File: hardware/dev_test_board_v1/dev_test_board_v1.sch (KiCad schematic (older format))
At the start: 52 parts, among them J1 USB_B_Micro, J2 Conn_SWD, J3 Conn_LCD, J4 Conn_GP, SW1 SW_SPDT, SW2 SW_PUSH, SW3 SW_PUSH, SW4 SW_PUSH, U1 STM32L031C4Tx, U2 FT230XS, U3 LIS2HH12, Y1 8MHz

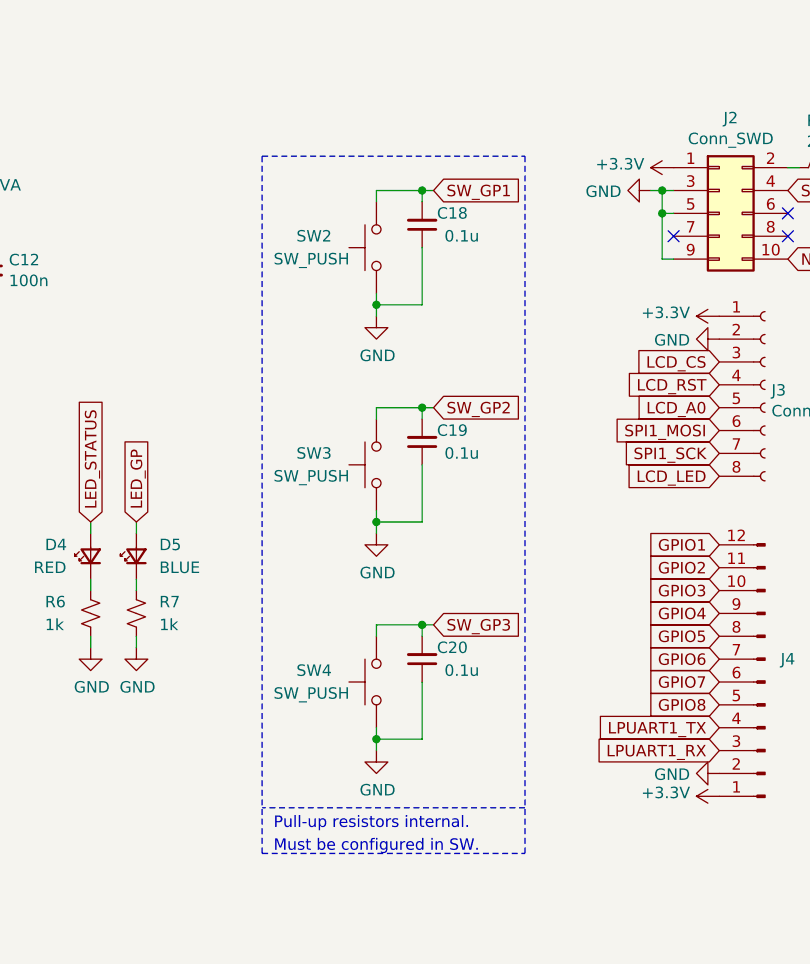
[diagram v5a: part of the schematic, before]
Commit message: Removed HW debouncing for SW2-4, finished routing.
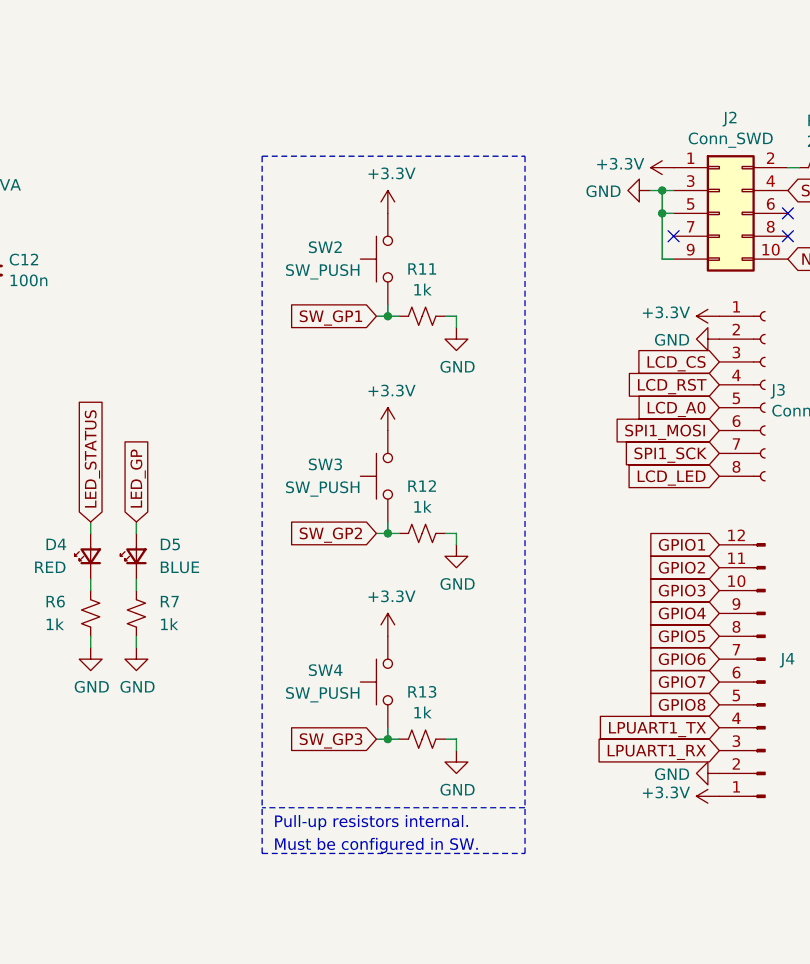
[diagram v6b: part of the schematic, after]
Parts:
- removed C18, C19, C20: 0.1u, Capacitor_SMD:C_0603_1608Metric, symbol Device:C_Small
- added R11, R12, R13: 1k, Resistor_SMD:R_0402_1005Metric, symbol Device:R_Small_US
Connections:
- net +3V3: now also SW2.2, SW3.2, SW4.2
- net GND: now also R11.1, R12.1, R13.1; no longer SW2.1, SW3.1, SW4.1
- net SW_GP1: now also SW2.1, R11.2; no longer SW2.2
- net SW_GP2: now also SW3.1, R12.2; no longer SW3.2
- net SW_GP3: now also SW4.1, R13.2; no longer SW4.2
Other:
- moved on the sheet: SW2
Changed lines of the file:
@@
 Text GLabel 10050 4700 0    50   Input ~ 0
 GPIO1
-Text GLabel 8800 5050 2    50   Input ~ 0
-SW_GP3
-$Comp
-L power:GND #PWR0140
-U 1 1 60A74DE7
-P 8550 5600
-F 0 "#PWR0140" H 8550 5350 50  0001 C CNN
-F 1 "GND" H 8555 5427 50  0000 C CNN
-F 2 "" H 8550 5600 50  0001 C CNN
-F 3 "" H 8550 5600 50  0001 C CNN
-	1    8550 5600
-	1    0    0    -1
-$EndComp
-Connection ~ 8550 5550
-Wire Wire Line
-	8550 5550 8550 5600
-Wire Wire Line
-	8750 5550 8550 5550
-Wire Wire Line
-	8750 5300 8750 5550
-Connection ~ 8750 5050
-Wire Wire Line
-	8750 5050 8800 5050
-Wire Wire Line
-	8750 5050 8750 5100
-Wire Wire Line
-	8550 5050 8750 5050
-Wire Wire Line
-	8550 5100 8550 5050
-Wire Wire Line
-	8550 5500 8550 5550
-$Comp
-L Switch:SW_Push SW4
-U 1 1 60A74DD7
-P 8550 5300
-F 0 "SW4" V 8600 5650 50  0000 R CNN
-F 1 "SW_PUSH" V 8500 5750 50  0000 R CNN
-F 2 "Button_Switch_SMD:SW_Push_1P1T_NO_6x6mm_H9.5mm" H 8550 5500 50  0001 C CNN
-F 3 "~" H 8550 5500 50  0001 C CNN
-	1    8550 5300
-	0    -1   -1   0
-$EndComp
-$Comp
-L Device:C_Small C20
-U 1 1 60A74DD1
-P 8750 5200
-F 0 "C20" H 8550 5150 50  0000 L CNN
-F 1 "0.1u" H 8500 5250 50  0000 L CNN
-F 2 "Capacitor_SMD:C_0603_1608Metric" H 8750 5200 50  0001 C CNN
-F 3 "~" H 8750 5200 50  0001 C CNN
-	1    8750 5200
-	-1   0    0    1
-$EndComp
-Text GLabel 8800 4100 2    50   Input ~ 0
-SW_GP2
-$Comp
-L power:GND #PWR0139
-U 1 1 60A5AFB5
-P 8550 4650
-F 0 "#PWR0139" H 8550 4400 50  0001 C CNN
-F 1 "GND" H 8555 4477 50  0000 C CNN
-F 2 "" H 8550 4650 50  0001 C CNN
-F 3 "" H 8550 4650 50  0001 C CNN
-	1    8550 4650
-	1    0    0    -1
-$EndComp
-Connection ~ 8550 4600
-Wire Wire Line
-	8550 4600 8550 4650
-Wire Wire Line
-	8750 4600 8550 4600
-Wire Wire Line
-	8750 4350 8750 4600
-Connection ~ 8750 4100
-Wire Wire Line
-	8750 4100 8800 4100
-Wire Wire Line
-	8750 4100 8750 4150
-Wire Wire Line
-	8550 4100 8750 4100
-Wire Wire Line
-	8550 4150 8550 4100
-Wire Wire Line
-	8550 4550 8550 4600
-$Comp
-L Switch:SW_Push SW3
-U 1 1 60A5AFA5
-P 8550 4350
-F 0 "SW3" V 8600 4700 50  0000 R CNN
-F 1 "SW_PUSH" V 8500 4800 50  0000 R CNN
-F 2 "Button_Switch_SMD:SW_Push_1P1T_NO_6x6mm_H9.5mm" H 8550 4550 50  0001 C CNN
-F 3 "~" H 8550 4550 50  0001 C CNN
-	1    8550 4350
-	0    -1   -1   0
-$EndComp
-$Comp
-L Device:C_Small C19
-U 1 1 60A5AF9F
-P 8750 4250
-F 0 "C19" H 8550 4200 50  0000 L CNN
-F 1 "0.1u" H 8500 4300 50  0000 L CNN
-F 2 "Capacitor_SMD:C_0603_1608Metric" H 8750 4250 50  0001 C CNN
-F 3 "~" H 8750 4250 50  0001 C CNN
-	1    8750 4250
-	-1   0    0    1
-$EndComp
-Text GLabel 8800 3150 2    50   Input ~ 0
+Text GLabel 8550 3700 0    50   Input ~ 0
 SW_GP1
-$Comp
-L power:GND #PWR0138
-U 1 1 60A551CE
-P 8550 3700
-F 0 "#PWR0138" H 8550 3450 50  0001 C CNN
-F 1 "GND" H 8555 3527 50  0000 C CNN
-F 2 "" H 8550 3700 50  0001 C CNN
-F 3 "" H 8550 3700 50  0001 C CNN
-	1    8550 3700
-	1    0    0    -1
-$EndComp
-Connection ~ 8550 3650
-Wire Wire Line
-	8550 3650 8550 3700
-Wire Wire Line
-	8750 3650 8550 3650
-Wire Wire Line
-	8750 3400 8750 3650
-Connection ~ 8750 3150
-Wire Wire Line
-	8750 3150 8800 3150
-Wire Wire Line
-	8750 3150 8750 3200
-Wire Wire Line
-	8550 3150 8750 3150
-Wire Wire Line
-	8550 3200 8550 3150
-Wire Wire Line
-	8550 3600 8550 3650
 $Comp
 L Switch:SW_Push SW2
 U 1 1 60A2B615
-P 8550 3400
-F 0 "SW2" V 8600 3750 50  0000 R CNN
-F 1 "SW_PUSH" V 8500 3850 50  0000 R CNN
-F 2 "Button_Switch_SMD:SW_Push_1P1T_NO_6x6mm_H9.5mm" H 8550 3600 50  0001 C CNN
-F 3 "~" H 8550 3600 50  0001 C CNN
-	1    8550 3400
+P 8600 3450
+F 0 "SW2" V 8650 3800 50  0000 R CNN
+F 1 "SW_PUSH" V 8550 3900 50  0000 R CNN
+F 2 "Button_Switch_SMD:SW_Push_1P1T_NO_6x6mm_H9.5mm" H 8600 3650 50  0001 C CNN
+F 3 "~" H 8600 3650 50  0001 C CNN
+	1    8600 3450
 	0    -1   -1   0
 $EndComp
@@
 	1    9850 3050
 	0    -1   -1   0
-$EndComp
-$Comp
-L Device:C_Small C18
-U 1 1 609CE345
-P 8750 3300
-F 0 "C18" H 8550 3250 50  0000 L CNN
-F 1 "0.1u" H 8500 3350 50  0000 L CNN
-F 2 "Capacitor_SMD:C_0603_1608Metric" H 8750 3300 50  0001 C CNN
-F 3 "~" H 8750 3300 50  0001 C CNN
-	1    8750 3300
-	-1   0    0    1
 $EndComp
 Text GLabel 10350 3450 2    50   Input ~ 0
@@
 Wire Wire Line
 	3100 1300 3100 1400
+$Comp
+L power:+3.3V #PWR0139
+U 1 1 60A33A90
+P 8600 3250
+F 0 "#PWR0139" H 8600 3100 50  0001 C CNN
+F 1 "+3.3V" H 8615 3423 50  0000 C CNN
+F 2 "" H 8600 3250 50  0001 C CNN
+F 3 "" H 8600 3250 50  0001 C CNN
+	1    8600 3250
+	1    0    0    -1
+$EndComp
+Wire Wire Line
+	8600 3650 8600 3700
+Wire Wire Line
+	8600 3700 8650 3700
+Wire Wire Line
+	8850 3700 8900 3700
+Wire Wire Line
+	8900 3700 8900 3750
+$Comp
+L power:GND #PWR0140
+U 1 1 60A5CE5A
+P 8900 3750
+F 0 "#PWR0140" H 8900 3500 50  0001 C CNN
+F 1 "GND" H 8905 3577 50  0000 C CNN
+F 2 "" H 8900 3750 50  0001 C CNN
+F 3 "" H 8900 3750 50  0001 C CNN
+	1    8900 3750
+	1    0    0    -1
+$EndComp
+Text GLabel 8550 4650 0    50   Input ~ 0
+SW_GP2
+$Comp
+L Switch:SW_Push SW3
+U 1 1 60A82445
+P 8600 4400
+F 0 "SW3" V 8650 4750 50  0000 R CNN
+F 1 "SW_PUSH" V 8550 4850 50  0000 R CNN
+F 2 "Button_Switch_SMD:SW_Push_1P1T_NO_6x6mm_H9.5mm" H 8600 4600 50  0001 C CNN
+F 3 "~" H 8600 4600 50  0001 C CNN
+	1    8600 4400
+	0    -1   -1   0
+$EndComp
+$Comp
+L power:+3.3V #PWR0146
+U 1 1 60A8244B
+P 8600 4200
+F 0 "#PWR0146" H 8600 4050 50  0001 C CNN
+F 1 "+3.3V" H 8615 4373 50  0000 C CNN
+F 2 "" H 8600 4200 50  0001 C CNN
+F 3 "" H 8600 4200 50  0001 C CNN
+	1    8600 4200
+	1    0    0    -1
+$EndComp
+Wire Wire Line
+	8600 4600 8600 4650
+Wire Wire Line
+	8600 4650 8650 4650
+Connection ~ 8600 4650
+$Comp
+L Device:R_Small_US R12
+U 1 1 60A82455
+P 8750 4650
+F 0 "R12" V 8545 4650 50  0000 C CNN
+F 1 "1k" V 8636 4650 50  0000 C CNN
+F 2 "Resistor_SMD:R_0402_1005Metric" H 8750 4650 50  0001 C CNN
+F 3 "~" H 8750 4650 50  0001 C CNN
+	1    8750 4650
+	0    1    1    0
+$EndComp
+Wire Wire Line
+	8850 4650 8900 4650
+Wire Wire Line
+	8900 4650 8900 4700
+$Comp
+L power:GND #PWR0147
+U 1 1 60A8245D
+P 8900 4700
+F 0 "#PWR0147" H 8900 4450 50  0001 C CNN
+F 1 "GND" H 8905 4527 50  0000 C CNN
+F 2 "" H 8900 4700 50  0001 C CNN
+F 3 "" H 8900 4700 50  0001 C CNN
+	1    8900 4700
+	1    0    0    -1
+$EndComp
+Text GLabel 8550 5550 0    50   Input ~ 0
+SW_GP3
+$Comp
+L Switch:SW_Push SW4
+U 1 1 60A9BB90
+P 8600 5300
+F 0 "SW4" V 8650 5650 50  0000 R CNN
+F 1 "SW_PUSH" V 8550 5750 50  0000 R CNN
+F 2 "Button_Switch_SMD:SW_Push_1P1T_NO_6x6mm_H9.5mm" H 8600 5500 50  0001 C CNN
+F 3 "~" H 8600 5500 50  0001 C CNN
+	1    8600 5300
+	0    -1   -1   0
+$EndComp
+$Comp
+L power:+3.3V #PWR0149
+U 1 1 60A9BB96
+P 8600 5100
+F 0 "#PWR0149" H 8600 4950 50  0001 C CNN
+F 1 "+3.3V" H 8615 5273 50  0000 C CNN
+F 2 "" H 8600 5100 50  0001 C CNN
+F 3 "" H 8600 5100 50  0001 C CNN
+	1    8600 5100
+	1    0    0    -1
+$EndComp
+Wire Wire Line
+	8600 5500 8600 5550
+Wire Wire Line
+	8600 5550 8650 5550
+Connection ~ 8600 5550
+$Comp
+L Device:R_Small_US R13
+U 1 1 60A9BBA0
+P 8750 5550
+F 0 "R13" V 8545 5550 50  0000 C CNN
+F 1 "1k" V 8636 5550 50  0000 C CNN
+F 2 "Resistor_SMD:R_0402_1005Metric" H 8750 5550 50  0001 C CNN
+F 3 "~" H 8750 5550 50  0001 C CNN
+	1    8750 5550
+	0    1    1    0
+$EndComp
+Wire Wire Line
+	8850 5550 8900 5550
+Wire Wire Line
+	8900 5550 8900 5600
+$Comp
+L power:GND #PWR0150
+U 1 1 60A9BBA8
+P 8900 5600
+F 0 "#PWR0150" H 8900 5350 50  0001 C CNN
+F 1 "GND" H 8905 5427 50  0000 C CNN
+F 2 "" H 8900 5600 50  0001 C CNN
+F 3 "" H 8900 5600 50  0001 C CNN
+	1    8900 5600
+	1    0    0    -1
+$EndComp
+$Comp
+L Device:R_Small_US R11
+U 1 1 60ADC002
+P 8750 3700
+F 0 "R11" V 8545 3700 50  0000 C CNN
+F 1 "1k" V 8636 3700 50  0000 C CNN
+F 2 "Resistor_SMD:R_0402_1005Metric" H 8750 3700 50  0001 C CNN
+F 3 "~" H 8750 3700 50  0001 C CNN
+	1    8750 3700
+	0    1    1    0
+$EndComp
+Wire Wire Line
+	8600 3700 8550 3700
+Connection ~ 8600 3700
+Wire Wire Line
+	8600 4650 8550 4650
+Wire Wire Line
+	8600 5550 8550 5550
 $EndSCHEMATC

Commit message: Routing cleaned up a bit and PCBs ordered.
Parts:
- C1: LCSC (none) -> C57112; LCSC Part # (none) -> C57112
- C10, C12, C16, C17, C3, C4, C8, C9: LCSC (none) -> C1525; LCSC Part # (none) -> C1525
- C11: LCSC (none) -> C52923; LCSC Part # (none) -> C52923
- C13, C14: LCSC (none) -> C30274; LCSC Part # (none) -> C30274
- C15, C7: LCSC (none) -> C15525; LCSC Part # (none) -> C15525
- C5, C6: LCSC (none) -> C1671; LCSC Part # (none) -> C1671
- D2: LCSC (none) -> C72038; LCSC Part # (none) -> C72038
- D3: LCSC (none) -> C72043; LCSC Part # (none) -> C72043
- D4: LCSC (none) -> C2286; LCSC Part # (none) -> C2286
- D5: LCSC (none) -> C72041; LCSC Part # (none) -> C72041
- FB1: LCSC (none) -> C1017; LCSC Part # (none) -> C1017
- L1: LCSC (none) -> C12100; LCSC Part # (none) -> C12100
- R1, R2: footprint Resistor_SMD:R_0402_1005Metric -> Resistor_SMD:R_0603_1608Metric; LCSC (none) -> C25190; LCSC Part # (none) -> C25190
- R10: LCSC (none) -> C25092; LCSC Part # (none) -> C25092
- R11, R12, R13: LCSC (none) -> C11702; LCSC Part # (none) -> C11702
- R3, R4: LCSC (none) -> C22966; LCSC Part # (none) -> C22966
- R5: LCSC (none) -> C25744; LCSC Part # (none) -> C25744
- R6, R7: LCSC (none) -> C21190; LCSC Part # (none) -> C21190
- R8, R9: LCSC (none) -> C25900; LCSC Part # (none) -> C25900
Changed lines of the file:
@@
 F 2 "Capacitor_SMD:C_0603_1608Metric" H 2300 1500 50  0001 C CNN
 F 3 "~" H 2300 1500 50  0001 C CNN
+F 4 "C57112" H 2300 1500 50  0001 C CNN "LCSC Part #"
+F 5 "C57112" H 2300 1500 50  0001 C CNN "LCSC"
 	1    2300 1500
 	1    0    0    -1
@@
 F 2 "Capacitor_SMD:C_0402_1005Metric" H 3100 1500 50  0001 C CNN
 F 3 "~" H 3100 1500 50  0001 C CNN
+F 4 "C1525" H 3100 1500 50  0001 C CNN "LCSC Part #"
+F 5 "C1525" H 3100 1500 50  0001 C CNN "LCSC"
 	1    3100 1500
 	1    0    0    -1
@@
 F 2 "Capacitor_SMD:C_0402_1005Metric" H 4150 1050 50  0001 C CNN
 F 3 "~" H 4150 1050 50  0001 C CNN
+F 4 "C1525" H 4150 1050 50  0001 C CNN "LCSC Part #"
+F 5 "C1525" H 4150 1050 50  0001 C CNN "LCSC"
 	1    4150 1050
 	-1   0    0    1
@@
 F 2 "Capacitor_SMD:C_0402_1005Metric" H 1650 4400 50  0001 C CNN
 F 3 "~" H 1650 4400 50  0001 C CNN
+F 4 "C15525" H 1650 4400 50  0001 C CNN "LCSC Part #"
+F 5 "C15525" H 1650 4400 50  0001 C CNN "LCSC"
 	1    1650 4400
 	1    0    0    -1
@@
 F 2 "Capacitor_SMD:C_0402_1005Metric" H 2000 4400 50  0001 C CNN
 F 3 "~" H 2000 4400 50  0001 C CNN
+F 4 "C1525" H 2000 4400 50  0001 C CNN "LCSC Part #"
+F 5 "C1525" H 2000 4400 50  0001 C CNN "LCSC"
 	1    2000 4400
 	1    0    0    -1
@@
 F 2 "Capacitor_SMD:C_0402_1005Metric" H 2350 4400 50  0001 C CNN
 F 3 "~" H 2350 4400 50  0001 C CNN
+F 4 "C1525" H 2350 4400 50  0001 C CNN "LCSC Part #"
+F 5 "C1525" H 2350 4400 50  0001 C CNN "LCSC"
 	1    2350 4400
 	1    0    0    -1
@@
 F 2 "Resistor_SMD:R_0402_1005Metric" H 1450 5300 50  0001 C CNN
 F 3 "~" H 1450 5300 50  0001 C CNN
+F 4 "C25900" H 1450 5300 50  0001 C CNN "LCSC Part #"
+F 5 "C25900" H 1450 5300 50  0001 C CNN "LCSC"
 	1    1450 5300
 	-1   0    0    1
@@
 F 2 "Resistor_SMD:R_0402_1005Metric" H 1450 5800 50  0001 C CNN
 F 3 "~" H 1450 5800 50  0001 C CNN
+F 4 "C25900" H 1450 5800 50  0001 C CNN "LCSC Part #"
+F 5 "C25900" H 1450 5800 50  0001 C CNN "LCSC"
 	1    1450 5800
 	-1   0    0    1
@@
 F 2 "Resistor_SMD:R_0603_1608Metric" H 6800 1500 50  0001 C CNN
 F 3 "~" H 6800 1500 50  0001 C CNN
+F 4 "C22966" H 6800 1500 50  0001 C CNN "LCSC Part #"
+F 5 "C22966" H 6800 1500 50  0001 C CNN "LCSC"
 	1    6800 1500
 	1    0    0    -1
@@
 F 2 "Resistor_SMD:R_0603_1608Metric" H 6600 1500 50  0001 C CNN
 F 3 "~" H 6600 1500 50  0001 C CNN
+F 4 "C22966" H 6600 1500 50  0001 C CNN "LCSC Part #"
+F 5 "C22966" H 6600 1500 50  0001 C CNN "LCSC"
 	1    6600 1500
 	1    0    0    -1
@@
 F 2 "LED_SMD:LED_0603_1608Metric" V 6600 1200 50  0001 C CNN
 F 3 "~" V 6600 1200 50  0001 C CNN
+F 4 "C72038" H 6600 1200 50  0001 C CNN "LCSC Part #"
+F 5 "C72038" H 6600 1200 50  0001 C CNN "LCSC"
 	1    6600 1200
 	0    -1   -1   0
@@
 F 2 "LED_SMD:LED_0603_1608Metric" V 6800 1200 50  0001 C CNN
 F 3 "~" V 6800 1200 50  0001 C CNN
+F 4 "C72043" H 6800 1200 50  0001 C CNN "LCSC Part #"
+F 5 "C72043" H 6800 1200 50  0001 C CNN "LCSC"
 	1    6800 1200
 	0    -1   -1   0
@@
 F 2 "Capacitor_SMD:C_0402_1005Metric" H 3750 6100 50  0001 C CNN
 F 3 "~" H 3750 6100 50  0001 C CNN
+F 4 "C30274" H 3750 6100 50  0001 C CNN "LCSC Part #"
+F 5 "C30274" H 3750 6100 50  0001 C CNN "LCSC"
 	1    3750 6100
 	1    0    0    -1
@@
 F 2 "Capacitor_SMD:C_0402_1005Metric" H 4150 6100 50  0001 C CNN
 F 3 "~" H 4150 6100 50  0001 C CNN
+F 4 "C30274" H 4150 6100 50  0001 C CNN "LCSC Part #"
+F 5 "C30274" H 4150 6100 50  0001 C CNN "LCSC"
 	1    4150 6100
 	1    0    0    -1
@@
 F 2 "Inductor_SMD:L_0603_1608Metric" H 6300 3350 50  0001 C CNN
 F 3 "~" H 6300 3350 50  0001 C CNN
+F 4 "C12100" H 6300 3350 50  0001 C CNN "LCSC Part #"
+F 5 "C12100" H 6300 3350 50  0001 C CNN "LCSC"
 	1    6300 3350
 	0    1    1    0
@@
 F 2 "Capacitor_SMD:C_0402_1005Metric" H 6850 3500 50  0001 C CNN
 F 3 "~" H 6850 3500 50  0001 C CNN
+F 4 "C1525" H 6850 3500 50  0001 C CNN "LCSC Part #"
+F 5 "C1525" H 6850 3500 50  0001 C CNN "LCSC"
 	1    6850 3500
 	1    0    0    -1
@@
 F 2 "Capacitor_SMD:C_0402_1005Metric" H 5700 3350 50  0001 C CNN
 F 3 "~" H 5700 3350 50  0001 C CNN
+F 4 "C1525" H 5700 3350 50  0001 C CNN "LCSC Part #"
+F 5 "C1525" H 5700 3350 50  0001 C CNN "LCSC"
 	1    5700 3350
 	1    0    0    -1
@@
 F 2 "Capacitor_SMD:C_0402_1005Metric" H 5350 3350 50  0001 C CNN
 F 3 "~" H 5350 3350 50  0001 C CNN
+F 4 "C1525" H 5350 3350 50  0001 C CNN "LCSC Part #"
+F 5 "C1525" H 5350 3350 50  0001 C CNN "LCSC"
 	1    5350 3350
 	1    0    0    -1
@@
 F 2 "Capacitor_SMD:C_0402_1005Metric" H 5000 3350 50  0001 C CNN
 F 3 "~" H 5000 3350 50  0001 C CNN
+F 4 "C1525" H 5000 3350 50  0001 C CNN "LCSC Part #"
+F 5 "C1525" H 5000 3350 50  0001 C CNN "LCSC"
 	1    5000 3350
 	1    0    0    -1
@@
 F 2 "Capacitor_SMD:C_0402_1005Metric" H 4650 3350 50  0001 C CNN
 F 3 "~" H 4650 3350 50  0001 C CNN
+F 4 "C15525" H 4650 3350 50  0001 C CNN "LCSC Part #"
+F 5 "C15525" H 4650 3350 50  0001 C CNN "LCSC"
 	1    4650 3350
 	1    0    0    -1
@@
 F 2 "LED_SMD:LED_0603_1608Metric" V 7300 4750 50  0001 C CNN
 F 3 "~" V 7300 4750 50  0001 C CNN
+F 4 "C2286" H 7300 4750 50  0001 C CNN "LCSC Part #"
+F 5 "C2286" H 7300 4750 50  0001 C CNN "LCSC"
 	1    7300 4750
 	0    -1   -1   0
@@
 F 2 "Resistor_SMD:R_0603_1608Metric" H 7300 5000 50  0001 C CNN
 F 3 "~" H 7300 5000 50  0001 C CNN
+F 4 "C21190" H 7300 5000 50  0001 C CNN "LCSC Part #"
+F 5 "C21190" H 7300 5000 50  0001 C CNN "LCSC"
 	1    7300 5000
 	1    0    0    -1
@@
 F 2 "LED_SMD:LED_0603_1608Metric" V 7500 4750 50  0001 C CNN
 F 3 "~" V 7500 4750 50  0001 C CNN
+F 4 "C72041" H 7500 4750 50  0001 C CNN "LCSC Part #"
+F 5 "C72041" H 7500 4750 50  0001 C CNN "LCSC"
 	1    7500 4750
 	0    -1   -1   0
@@
 F 2 "Resistor_SMD:R_0603_1608Metric" H 7500 5000 50  0001 C CNN
 F 3 "~" H 7500 5000 50  0001 C CNN
+F 4 "C21190" H 7500 5000 50  0001 C CNN "LCSC Part #"
+F 5 "C21190" H 7500 5000 50  0001 C CNN "LCSC"
 	1    7500 5000
 	1    0    0    -1
@@
 F 2 "Resistor_SMD:R_0402_1005Metric" H 3800 4500 50  0001 C CNN
 F 3 "~" H 3800 4500 50  0001 C CNN
+F 4 "C25744" H 3800 4500 50  0001 C CNN "LCSC Part #"
+F 5 "C25744" H 3800 4500 50  0001 C CNN "LCSC"
 	1    3800 4500
 	0    1    1    0
@@
 F 2 "Resistor_SMD:R_0402_1005Metric" H 10500 3050 50  0001 C CNN
 F 3 "~" H 10500 3050 50  0001 C CNN
+F 4 "C25092" H 10500 3050 50  0001 C CNN "LCSC Part #"
+F 5 "C25092" H 10500 3050 50  0001 C CNN "LCSC"
 	1    10500 3050
 	0    1    1    0
@@
 F 2 "Capacitor_SMD:C_0402_1005Metric" H 6500 3500 50  0001 C CNN
 F 3 "~" H 6500 3500 50  0001 C CNN
+F 4 "C52923" H 6500 3500 50  0001 C CNN "LCSC Part #"
+F 5 "C52923" H 6500 3500 50  0001 C CNN "LCSC"
 	1    6500 3500
 	1    0    0    -1
@@
 F 0 "R2" V 2800 2700 50  0000 C CNN
 F 1 "27R" V 2900 2700 50  0000 C CNN
-F 2 "Resistor_SMD:R_0402_1005Metric" H 2700 2700 50  0001 C CNN
+F 2 "Resistor_SMD:R_0603_1608Metric" H 2700 2700 50  0001 C CNN
 F 3 "~" H 2700 2700 50  0001 C CNN
+F 4 "C25190" H 2700 2700 50  0001 C CNN "LCSC Part #"
+F 5 "C25190" H 2700 2700 50  0001 C CNN "LCSC"
 	1    2700 2700
 	0    1    1    0
@@
 F 0 "R1" V 2495 2550 50  0000 C CNN
 F 1 "27R" V 2586 2550 50  0000 C CNN
-F 2 "Resistor_SMD:R_0402_1005Metric" H 2700 2550 50  0001 C CNN
+F 2 "Resistor_SMD:R_0603_1608Metric" H 2700 2550 50  0001 C CNN
 F 3 "~" H 2700 2550 50  0001 C CNN
+F 4 "C25190" H 2700 2550 50  0001 C CNN "LCSC Part #"
+F 5 "C25190" H 2700 2550 50  0001 C CNN "LCSC"
 	1    2700 2550
 	0    1    1    0
@@
 F 2 "Capacitor_SMD:C_0603_1608Metric" H 2400 2350 50  0001 C CNN
 F 3 "~" H 2400 2350 50  0001 C CNN
+F 4 "C1671" H 2400 2350 50  0001 C CNN "LCSC Part #"
+F 5 "C1671" H 2400 2350 50  0001 C CNN "LCSC"
 	1    2400 2350
 	1    0    0    -1
@@
 F 2 "Capacitor_SMD:C_0603_1608Metric" H 2400 2900 50  0001 C CNN
 F 3 "~" H 2400 2900 50  0001 C CNN
+F 4 "C1671" H 2400 2900 50  0001 C CNN "LCSC Part #"
+F 5 "C1671" H 2400 2900 50  0001 C CNN "LCSC"
 	1    2400 2900
 	1    0    0    -1
@@
 F 2 "Inductor_SMD:L_0805_2012Metric" V 2480 1300 50  0001 C CNN
 F 3 "~" H 2550 1300 50  0001 C CNN
+F 4 "C1017" H 2550 1300 50  0001 C CNN "LCSC Part #"
+F 5 "C1017" H 2550 1300 50  0001 C CNN "LCSC"
 	1    2550 1300
 	0    1    1    0
@@
 F 2 "Resistor_SMD:R_0402_1005Metric" H 8750 4650 50  0001 C CNN
 F 3 "~" H 8750 4650 50  0001 C CNN
+F 4 "C11702" H 8750 4650 50  0001 C CNN "LCSC Part #"
+F 5 "C11702" H 8750 4650 50  0001 C CNN "LCSC"
 	1    8750 4650
 	0    1    1    0
@@
 F 2 "Resistor_SMD:R_0402_1005Metric" H 8750 5550 50  0001 C CNN
 F 3 "~" H 8750 5550 50  0001 C CNN
+F 4 "C11702" H 8750 5550 50  0001 C CNN "LCSC Part #"
+F 5 "C11702" H 8750 5550 50  0001 C CNN "LCSC"
 	1    8750 5550
 	0    1    1    0
@@
 F 2 "Resistor_SMD:R_0402_1005Metric" H 8750 3700 50  0001 C CNN
 F 3 "~" H 8750 3700 50  0001 C CNN
+F 4 "C11702" H 8750 3700 50  0001 C CNN "LCSC Part #"
+F 5 "C11702" H 8750 3700 50  0001 C CNN "LCSC"
 	1    8750 3700
 	0    1    1    0
